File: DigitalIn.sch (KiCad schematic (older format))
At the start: 4 parts, among them Q1 BC847

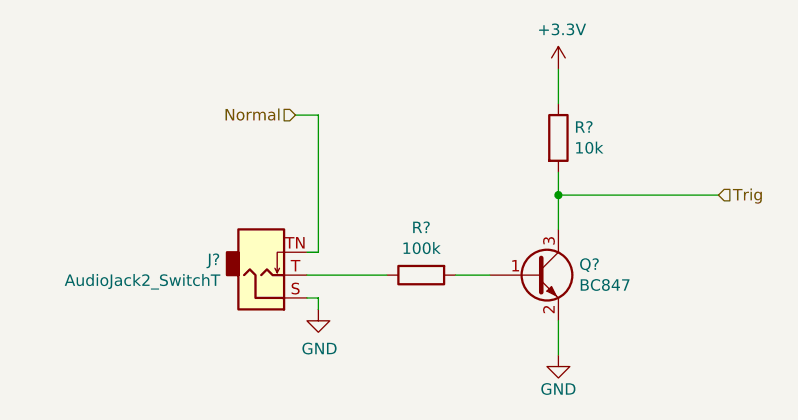
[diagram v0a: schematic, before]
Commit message: Added UI components.
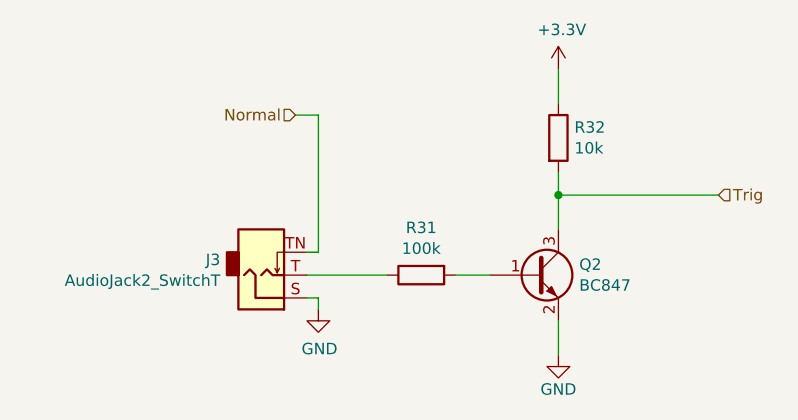
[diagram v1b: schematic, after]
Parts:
- gave numbers to parts that had none: 1
- renumbered Q1 to Q2, R20 to R31, R21 to R32
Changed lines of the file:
@@
 AR Path="/5DD41DD6/5D78C3C7/5C75FA5C" Ref="R?"  Part="1"
 AR Path="/5DD41DD6/5D7C6377/5C75FA5C" Ref="R?"  Part="1"
-AR Path="/5DE20ADD/5C75FA5C" Ref="R20"  Part="1"
-AR Path="/5E008663/5C75FA5C" Ref="R23"  Part="1"
+AR Path="/5DE20ADD/5C75FA5C" Ref="R?"  Part="1"
+AR Path="/5E008663/5C75FA5C" Ref="R?"  Part="1"
 AR Path="/5FF0E759/5DE20ADD/5C75FA5C" Ref="R?"  Part="1"
 AR Path="/5FF0E759/5E008663/5C75FA5C" Ref="R?"  Part="1"
 AR Path="/600106BC/5C75FA5C" Ref="R?"  Part="1"
 AR Path="/6001072A/5C75FA5C" Ref="R?"  Part="1"
-AR Path="/61E4E4E9/5C75FA5C" Ref="R?"  Part="1"
-F 0 "R?" V 4843 3900 50  0000 C CNN
+AR Path="/61E4E4E9/5C75FA5C" Ref="R31"  Part="1"
+F 0 "R31" V 4843 3900 50  0000 C CNN
 F 1 "100k" V 4934 3900 50  0000 C CNN
 F 2 "Resistor_SMD:R_0603_1608Metric" V 4980 3900 50  0001 C CNN
@@
 AR Path="/5DD41DD6/5D78C3C7/5C75FC51" Ref="#PWR?"  Part="1"
 AR Path="/5DD41DD6/5D7C6377/5C75FC51" Ref="#PWR?"  Part="1"
-AR Path="/5DE20ADD/5C75FC51" Ref="#PWR073"  Part="1"
-AR Path="/5E008663/5C75FC51" Ref="#PWR077"  Part="1"
+AR Path="/5DE20ADD/5C75FC51" Ref="#PWR?"  Part="1"
+AR Path="/5E008663/5C75FC51" Ref="#PWR?"  Part="1"
 AR Path="/5FF0E759/5DE20ADD/5C75FC51" Ref="#PWR?"  Part="1"
 AR Path="/5FF0E759/5E008663/5C75FC51" Ref="#PWR?"  Part="1"
 AR Path="/600106BC/5C75FC51" Ref="#PWR?"  Part="1"
 AR Path="/6001072A/5C75FC51" Ref="#PWR?"  Part="1"
-AR Path="/61E4E4E9/5C75FC51" Ref="#PWR?"  Part="1"
-F 0 "#PWR?" H 5650 4000 50  0001 C CNN
+AR Path="/61E4E4E9/5C75FC51" Ref="#PWR058"  Part="1"
+F 0 "#PWR058" H 5650 4000 50  0001 C CNN
 F 1 "GND" H 5650 4100 50  0000 C CNN
 F 2 "" H 5650 4250 50  0001 C CNN
@@
 AR Path="/5DD41DD6/5D78C3C7/5C75FCA9" Ref="R?"  Part="1"
 AR Path="/5DD41DD6/5D7C6377/5C75FCA9" Ref="R?"  Part="1"
-AR Path="/5DE20ADD/5C75FCA9" Ref="R21"  Part="1"
-AR Path="/5E008663/5C75FCA9" Ref="R24"  Part="1"
+AR Path="/5DE20ADD/5C75FCA9" Ref="R?"  Part="1"
+AR Path="/5E008663/5C75FCA9" Ref="R?"  Part="1"
 AR Path="/5FF0E759/5DE20ADD/5C75FCA9" Ref="R?"  Part="1"
 AR Path="/5FF0E759/5E008663/5C75FCA9" Ref="R?"  Part="1"
 AR Path="/600106BC/5C75FCA9" Ref="R?"  Part="1"
 AR Path="/6001072A/5C75FCA9" Ref="R?"  Part="1"
-AR Path="/61E4E4E9/5C75FCA9" Ref="R?"  Part="1"
-F 0 "R?" H 5720 3346 50  0000 L CNN
+AR Path="/61E4E4E9/5C75FCA9" Ref="R32"  Part="1"
+F 0 "R32" H 5720 3346 50  0000 L CNN
 F 1 "10k" H 5720 3255 50  0000 L CNN
 F 2 "Resistor_SMD:R_0603_1608Metric" V 5580 3300 50  0001 C CNN
@@
 AR Path="/5DD41DD6/5D78C3C7/5C074194" Ref="Q?"  Part="1"
 AR Path="/5DD41DD6/5D7C6377/5C074194" Ref="Q?"  Part="1"
-AR Path="/5DE20ADD/5C074194" Ref="Q1"  Part="1"
-AR Path="/5E008663/5C074194" Ref="Q3"  Part="1"
+AR Path="/5DE20ADD/5C074194" Ref="Q?"  Part="1"
+AR Path="/5E008663/5C074194" Ref="Q?"  Part="1"
 AR Path="/5FF0E759/5DE20ADD/5C074194" Ref="Q?"  Part="1"
 AR Path="/5FF0E759/5E008663/5C074194" Ref="Q?"  Part="1"
 AR Path="/600106BC/5C074194" Ref="Q?"  Part="1"
 AR Path="/6001072A/5C074194" Ref="Q?"  Part="1"
-AR Path="/61E4E4E9/5C074194" Ref="Q?"  Part="1"
-F 0 "Q?" H 5741 3946 50  0000 L CNN
+AR Path="/61E4E4E9/5C074194" Ref="Q2"  Part="1"
+F 0 "Q2" H 5741 3946 50  0000 L CNN
 F 1 "BC847" H 5741 3855 50  0000 L CNN
 F 2 "Package_TO_SOT_SMD:SOT-23" H 5750 3825 50  0001 L CIN
@@
 AR Path="/5DD41DD6/5D78C3C7/5CECEB5D" Ref="#PWR?"  Part="1"
 AR Path="/5DD41DD6/5D7C6377/5CECEB5D" Ref="#PWR?"  Part="1"
-AR Path="/5DE20ADD/5CECEB5D" Ref="#PWR072"  Part="1"
-AR Path="/5E008663/5CECEB5D" Ref="#PWR076"  Part="1"
+AR Path="/5DE20ADD/5CECEB5D" Ref="#PWR?"  Part="1"
+AR Path="/5E008663/5CECEB5D" Ref="#PWR?"  Part="1"
 AR Path="/5FF0E759/5DE20ADD/5CECEB5D" Ref="#PWR?"  Part="1"
 AR Path="/5FF0E759/5E008663/5CECEB5D" Ref="#PWR?"  Part="1"
 AR Path="/600106BC/5CECEB5D" Ref="#PWR?"  Part="1"
 AR Path="/6001072A/5CECEB5D" Ref="#PWR?"  Part="1"
-AR Path="/61E4E4E9/5CECEB5D" Ref="#PWR?"  Part="1"
-F 0 "#PWR?" H 5650 2850 50  0001 C CNN
+AR Path="/61E4E4E9/5CECEB5D" Ref="#PWR057"  Part="1"
+F 0 "#PWR057" H 5650 2850 50  0001 C CNN
 F 1 "+3.3V" H 5665 3173 50  0000 C CNN
 F 2 "" H 5650 3000 50  0001 C CNN
@@
 AR Path="/61E5BDEC" Ref="J?"  Part="1"
 AR Path="/61DB1EC2/61E5BDEC" Ref="J?"  Part="1"
-F 0 "J?" H 4171 3833 50  0000 R CNN
+AR Path="/61E4E4E9/61E5BDEC" Ref="J3"  Part="1"
+F 0 "J3" H 4171 3833 50  0000 R CNN
 F 1 "AudioJack2_SwitchT" H 4171 3924 50  0000 R CNN
 F 2 "Local:PJ398SM" H 4350 3900 50  0001 C CNN
@@
 AR Path="/61E5BDF2" Ref="#PWR?"  Part="1"
 AR Path="/61DB1EC2/61E5BDF2" Ref="#PWR?"  Part="1"
-F 0 "#PWR?" H 4600 3800 50  0001 C CNN
+AR Path="/61E4E4E9/61E5BDF2" Ref="#PWR056"  Part="1"
+F 0 "#PWR056" H 4600 3800 50  0001 C CNN
 F 1 "GND" H 4605 3877 50  0000 C CNN
 F 2 "" H 4600 4050 50  0001 C CNN

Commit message: Moved codec to audio module.
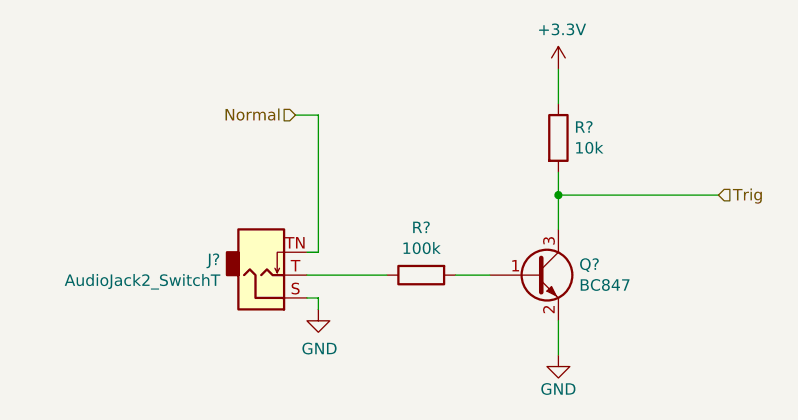
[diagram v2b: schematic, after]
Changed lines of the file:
@@
 AR Path="/6001072A/5C75FA5C" Ref="R?"  Part="1"
 AR Path="/61E4E4E9/5C75FA5C" Ref="R31"  Part="1"
-F 0 "R31" V 4843 3900 50  0000 C CNN
+AR Path="/621F67CE/5C75FA5C" Ref="R?"  Part="1"
+F 0 "R?" V 4843 3900 50  0000 C CNN
 F 1 "100k" V 4934 3900 50  0000 C CNN
 F 2 "Resistor_SMD:R_0603_1608Metric" V 4980 3900 50  0001 C CNN
@@
 AR Path="/6001072A/5C75FC51" Ref="#PWR?"  Part="1"
 AR Path="/61E4E4E9/5C75FC51" Ref="#PWR058"  Part="1"
-F 0 "#PWR058" H 5650 4000 50  0001 C CNN
+AR Path="/621F67CE/5C75FC51" Ref="#PWR?"  Part="1"
+F 0 "#PWR?" H 5650 4000 50  0001 C CNN
 F 1 "GND" H 5650 4100 50  0000 C CNN
 F 2 "" H 5650 4250 50  0001 C CNN
@@
 AR Path="/6001072A/5C75FCA9" Ref="R?"  Part="1"
 AR Path="/61E4E4E9/5C75FCA9" Ref="R32"  Part="1"
-F 0 "R32" H 5720 3346 50  0000 L CNN
+AR Path="/621F67CE/5C75FCA9" Ref="R?"  Part="1"
+F 0 "R?" H 5720 3346 50  0000 L CNN
 F 1 "10k" H 5720 3255 50  0000 L CNN
 F 2 "Resistor_SMD:R_0603_1608Metric" V 5580 3300 50  0001 C CNN
@@
 AR Path="/6001072A/5C074194" Ref="Q?"  Part="1"
 AR Path="/61E4E4E9/5C074194" Ref="Q2"  Part="1"
-F 0 "Q2" H 5741 3946 50  0000 L CNN
+AR Path="/621F67CE/5C074194" Ref="Q?"  Part="1"
+F 0 "Q?" H 5741 3946 50  0000 L CNN
 F 1 "BC847" H 5741 3855 50  0000 L CNN
 F 2 "Package_TO_SOT_SMD:SOT-23" H 5750 3825 50  0001 L CIN
@@
 AR Path="/6001072A/5CECEB5D" Ref="#PWR?"  Part="1"
 AR Path="/61E4E4E9/5CECEB5D" Ref="#PWR057"  Part="1"
-F 0 "#PWR057" H 5650 2850 50  0001 C CNN
+AR Path="/621F67CE/5CECEB5D" Ref="#PWR?"  Part="1"
+F 0 "#PWR?" H 5650 2850 50  0001 C CNN
 F 1 "+3.3V" H 5665 3173 50  0000 C CNN
 F 2 "" H 5650 3000 50  0001 C CNN
@@
 AR Path="/61DB1EC2/61E5BDEC" Ref="J?"  Part="1"
 AR Path="/61E4E4E9/61E5BDEC" Ref="J3"  Part="1"
-F 0 "J3" H 4171 3833 50  0000 R CNN
+AR Path="/621F67CE/61E5BDEC" Ref="J?"  Part="1"
+F 0 "J?" H 4171 3833 50  0000 R CNN
 F 1 "AudioJack2_SwitchT" H 4171 3924 50  0000 R CNN
 F 2 "Local:PJ398SM" H 4350 3900 50  0001 C CNN
@@
 AR Path="/61DB1EC2/61E5BDF2" Ref="#PWR?"  Part="1"
 AR Path="/61E4E4E9/61E5BDF2" Ref="#PWR056"  Part="1"
-F 0 "#PWR056" H 4600 3800 50  0001 C CNN
+AR Path="/621F67CE/61E5BDF2" Ref="#PWR?"  Part="1"
+F 0 "#PWR?" H 4600 3800 50  0001 C CNN
 F 1 "GND" H 4605 3877 50  0000 C CNN
 F 2 "" H 4600 4050 50  0001 C CNN

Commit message: Re-annotation.
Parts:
- renumbered R31 to R11, R32 to R12
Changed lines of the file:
@@
 $Descr A4 11693 8268
 encoding utf-8
-Sheet 6 6
+Sheet 4 11
 Title ""
 Date ""
@@
 AR Path="/600106BC/5C75FA5C" Ref="R?"  Part="1"
 AR Path="/6001072A/5C75FA5C" Ref="R?"  Part="1"
-AR Path="/61E4E4E9/5C75FA5C" Ref="R31"  Part="1"
-AR Path="/621F67CE/5C75FA5C" Ref="R?"  Part="1"
-F 0 "R?" V 4843 3900 50  0000 C CNN
+AR Path="/61E4E4E9/5C75FA5C" Ref="R11"  Part="1"
+AR Path="/621F67CE/5C75FA5C" Ref="R46"  Part="1"
+F 0 "R46" V 4843 3900 50  0000 C CNN
 F 1 "100k" V 4934 3900 50  0000 C CNN
 F 2 "Resistor_SMD:R_0603_1608Metric" V 4980 3900 50  0001 C CNN
@@
 AR Path="/600106BC/5C75FC51" Ref="#PWR?"  Part="1"
 AR Path="/6001072A/5C75FC51" Ref="#PWR?"  Part="1"
-AR Path="/61E4E4E9/5C75FC51" Ref="#PWR058"  Part="1"
-AR Path="/621F67CE/5C75FC51" Ref="#PWR?"  Part="1"
-F 0 "#PWR?" H 5650 4000 50  0001 C CNN
+AR Path="/61E4E4E9/5C75FC51" Ref="#PWR038"  Part="1"
+AR Path="/621F67CE/5C75FC51" Ref="#PWR078"  Part="1"
+F 0 "#PWR078" H 5650 4000 50  0001 C CNN
 F 1 "GND" H 5650 4100 50  0000 C CNN
 F 2 "" H 5650 4250 50  0001 C CNN
@@
 AR Path="/600106BC/5C75FCA9" Ref="R?"  Part="1"
 AR Path="/6001072A/5C75FCA9" Ref="R?"  Part="1"
-AR Path="/61E4E4E9/5C75FCA9" Ref="R32"  Part="1"
-AR Path="/621F67CE/5C75FCA9" Ref="R?"  Part="1"
-F 0 "R?" H 5720 3346 50  0000 L CNN
+AR Path="/61E4E4E9/5C75FCA9" Ref="R12"  Part="1"
+AR Path="/621F67CE/5C75FCA9" Ref="R47"  Part="1"
+F 0 "R47" H 5720 3346 50  0000 L CNN
 F 1 "10k" H 5720 3255 50  0000 L CNN
 F 2 "Resistor_SMD:R_0603_1608Metric" V 5580 3300 50  0001 C CNN
@@
 AR Path="/6001072A/5C074194" Ref="Q?"  Part="1"
 AR Path="/61E4E4E9/5C074194" Ref="Q2"  Part="1"
-AR Path="/621F67CE/5C074194" Ref="Q?"  Part="1"
-F 0 "Q?" H 5741 3946 50  0000 L CNN
+AR Path="/621F67CE/5C074194" Ref="Q3"  Part="1"
+F 0 "Q3" H 5741 3946 50  0000 L CNN
 F 1 "BC847" H 5741 3855 50  0000 L CNN
 F 2 "Package_TO_SOT_SMD:SOT-23" H 5750 3825 50  0001 L CIN
@@
 AR Path="/600106BC/5CECEB5D" Ref="#PWR?"  Part="1"
 AR Path="/6001072A/5CECEB5D" Ref="#PWR?"  Part="1"
-AR Path="/61E4E4E9/5CECEB5D" Ref="#PWR057"  Part="1"
-AR Path="/621F67CE/5CECEB5D" Ref="#PWR?"  Part="1"
-F 0 "#PWR?" H 5650 2850 50  0001 C CNN
+AR Path="/61E4E4E9/5CECEB5D" Ref="#PWR037"  Part="1"
+AR Path="/621F67CE/5CECEB5D" Ref="#PWR077"  Part="1"
+F 0 "#PWR077" H 5650 2850 50  0001 C CNN
 F 1 "+3.3V" H 5665 3173 50  0000 C CNN
 F 2 "" H 5650 3000 50  0001 C CNN
@@
 AR Path="/61DB1EC2/61E5BDEC" Ref="J?"  Part="1"
 AR Path="/61E4E4E9/61E5BDEC" Ref="J3"  Part="1"
-AR Path="/621F67CE/61E5BDEC" Ref="J?"  Part="1"
-F 0 "J?" H 4171 3833 50  0000 R CNN
+AR Path="/621F67CE/61E5BDEC" Ref="J12"  Part="1"
+F 0 "J12" H 4171 3833 50  0000 R CNN
 F 1 "AudioJack2_SwitchT" H 4171 3924 50  0000 R CNN
 F 2 "Local:PJ398SM" H 4350 3900 50  0001 C CNN
@@
 AR Path="/61E5BDF2" Ref="#PWR?"  Part="1"
 AR Path="/61DB1EC2/61E5BDF2" Ref="#PWR?"  Part="1"
-AR Path="/61E4E4E9/61E5BDF2" Ref="#PWR056"  Part="1"
-AR Path="/621F67CE/61E5BDF2" Ref="#PWR?"  Part="1"
-F 0 "#PWR?" H 4600 3800 50  0001 C CNN
+AR Path="/61E4E4E9/61E5BDF2" Ref="#PWR036"  Part="1"
+AR Path="/621F67CE/61E5BDF2" Ref="#PWR076"  Part="1"
+F 0 "#PWR076" H 4600 3800 50  0001 C CNN
 F 1 "GND" H 4605 3877 50  0000 C CNN
 F 2 "" H 4600 4050 50  0001 C CNN

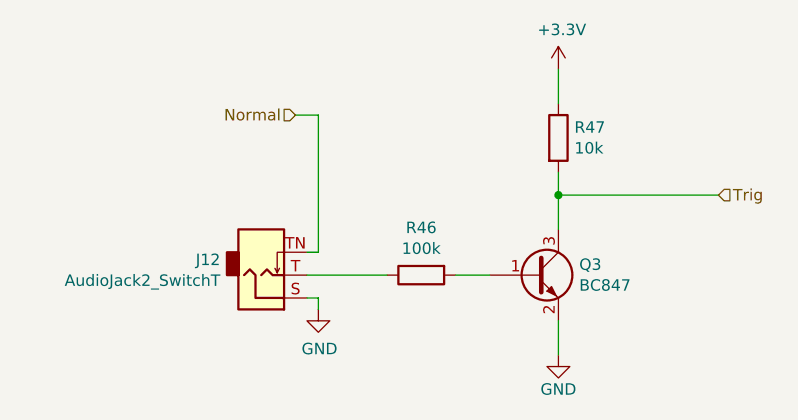
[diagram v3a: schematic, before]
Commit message: Assigned pins and cleared schema rules.
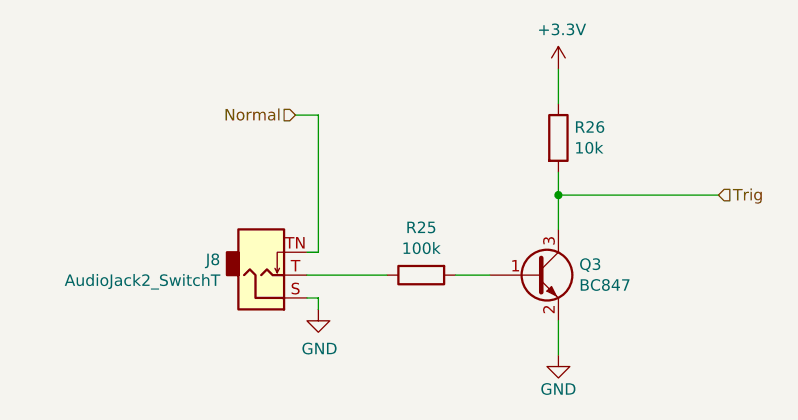
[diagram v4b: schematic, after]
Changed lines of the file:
@@
 $Descr A4 11693 8268
 encoding utf-8
-Sheet 4 11
+Sheet 6 11
 Title ""
 Date ""
@@
 AR Path="/6001072A/5C75FA5C" Ref="R?"  Part="1"
 AR Path="/61E4E4E9/5C75FA5C" Ref="R11"  Part="1"
-AR Path="/621F67CE/5C75FA5C" Ref="R46"  Part="1"
-F 0 "R46" V 4843 3900 50  0000 C CNN
+AR Path="/621F67CE/5C75FA5C" Ref="R25"  Part="1"
+F 0 "R25" V 4843 3900 50  0000 C CNN
 F 1 "100k" V 4934 3900 50  0000 C CNN
 F 2 "Resistor_SMD:R_0603_1608Metric" V 4980 3900 50  0001 C CNN
@@
 AR Path="/600106BC/5C75FC51" Ref="#PWR?"  Part="1"
 AR Path="/6001072A/5C75FC51" Ref="#PWR?"  Part="1"
-AR Path="/61E4E4E9/5C75FC51" Ref="#PWR038"  Part="1"
-AR Path="/621F67CE/5C75FC51" Ref="#PWR078"  Part="1"
-F 0 "#PWR078" H 5650 4000 50  0001 C CNN
+AR Path="/61E4E4E9/5C75FC51" Ref="#PWR040"  Part="1"
+AR Path="/621F67CE/5C75FC51" Ref="#PWR053"  Part="1"
+F 0 "#PWR053" H 5650 4000 50  0001 C CNN
 F 1 "GND" H 5650 4100 50  0000 C CNN
 F 2 "" H 5650 4250 50  0001 C CNN
@@
 AR Path="/6001072A/5C75FCA9" Ref="R?"  Part="1"
 AR Path="/61E4E4E9/5C75FCA9" Ref="R12"  Part="1"
-AR Path="/621F67CE/5C75FCA9" Ref="R47"  Part="1"
-F 0 "R47" H 5720 3346 50  0000 L CNN
+AR Path="/621F67CE/5C75FCA9" Ref="R26"  Part="1"
+F 0 "R26" H 5720 3346 50  0000 L CNN
 F 1 "10k" H 5720 3255 50  0000 L CNN
 F 2 "Resistor_SMD:R_0603_1608Metric" V 5580 3300 50  0001 C CNN
@@
 AR Path="/600106BC/5CECEB5D" Ref="#PWR?"  Part="1"
 AR Path="/6001072A/5CECEB5D" Ref="#PWR?"  Part="1"
-AR Path="/61E4E4E9/5CECEB5D" Ref="#PWR037"  Part="1"
-AR Path="/621F67CE/5CECEB5D" Ref="#PWR077"  Part="1"
-F 0 "#PWR077" H 5650 2850 50  0001 C CNN
+AR Path="/61E4E4E9/5CECEB5D" Ref="#PWR039"  Part="1"
+AR Path="/621F67CE/5CECEB5D" Ref="#PWR052"  Part="1"
+F 0 "#PWR052" H 5650 2850 50  0001 C CNN
 F 1 "+3.3V" H 5665 3173 50  0000 C CNN
 F 2 "" H 5650 3000 50  0001 C CNN
@@
 AR Path="/61DB1EC2/61E5BDEC" Ref="J?"  Part="1"
 AR Path="/61E4E4E9/61E5BDEC" Ref="J3"  Part="1"
-AR Path="/621F67CE/61E5BDEC" Ref="J12"  Part="1"
-F 0 "J12" H 4171 3833 50  0000 R CNN
+AR Path="/621F67CE/61E5BDEC" Ref="J8"  Part="1"
+F 0 "J8" H 4171 3833 50  0000 R CNN
 F 1 "AudioJack2_SwitchT" H 4171 3924 50  0000 R CNN
 F 2 "Local:PJ398SM" H 4350 3900 50  0001 C CNN
@@
 AR Path="/61E5BDF2" Ref="#PWR?"  Part="1"
 AR Path="/61DB1EC2/61E5BDF2" Ref="#PWR?"  Part="1"
-AR Path="/61E4E4E9/61E5BDF2" Ref="#PWR036"  Part="1"
-AR Path="/621F67CE/61E5BDF2" Ref="#PWR076"  Part="1"
-F 0 "#PWR076" H 4600 3800 50  0001 C CNN
+AR Path="/61E4E4E9/61E5BDF2" Ref="#PWR038"  Part="1"
+AR Path="/621F67CE/61E5BDF2" Ref="#PWR051"  Part="1"
+F 0 "#PWR051" H 4600 3800 50  0001 C CNN
 F 1 "GND" H 4605 3877 50  0000 C CNN
 F 2 "" H 4600 4050 50  0001 C CNN
